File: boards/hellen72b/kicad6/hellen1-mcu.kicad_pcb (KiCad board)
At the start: 2 copper layers, 46.5 x 37.3 mm, 91 parts, among them J101 TC2030-IDC-NL, J102 Net Tie, M101 Module:mcu/0.1, U101 AMS1117-3.3, U102 LMV324IPWR, U103 AP2337SA-7, U104 LMV324IPWR, U105 STM32F427IGT6, U106 LMV324IPWR, U107 LMV324IPWR, U108 LMV324IPWR, U109 LMV324IPWR, U111 XC6206P332MR, Y101 32.768 kHz, Y102 8.0 MHz

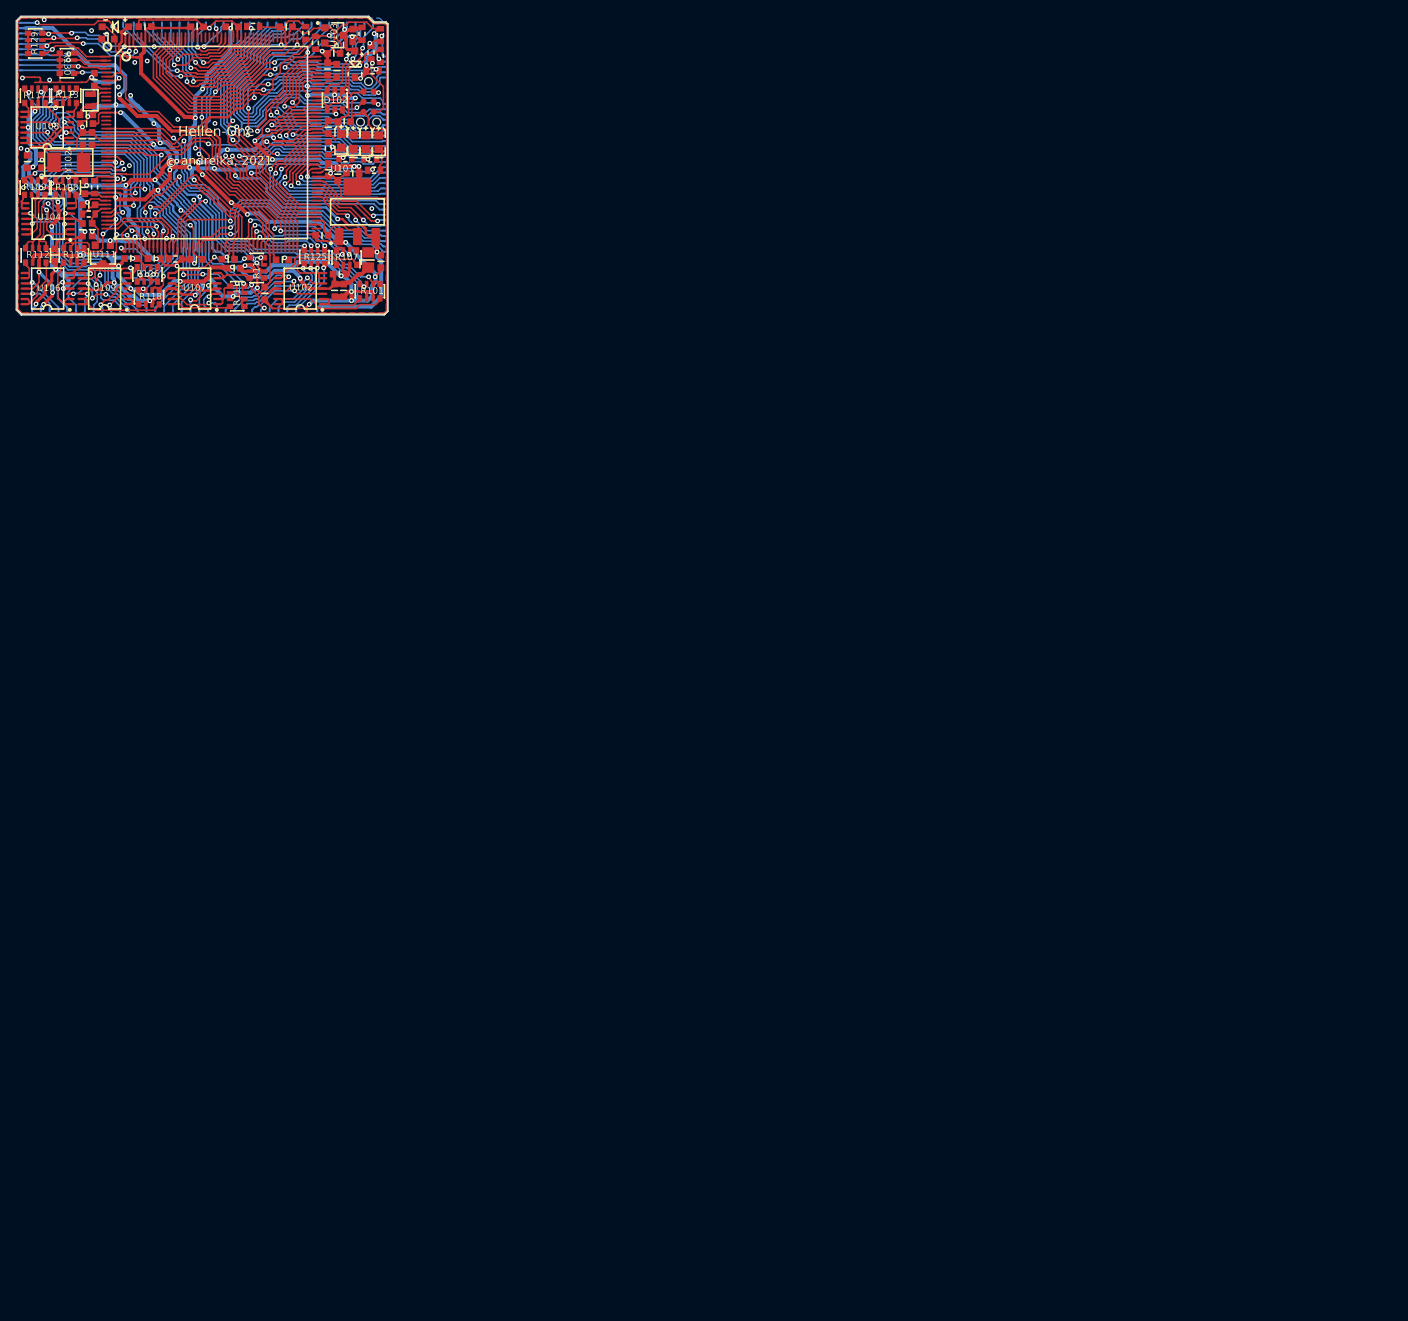
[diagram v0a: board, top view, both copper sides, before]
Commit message: update exported kicad files after refactoring
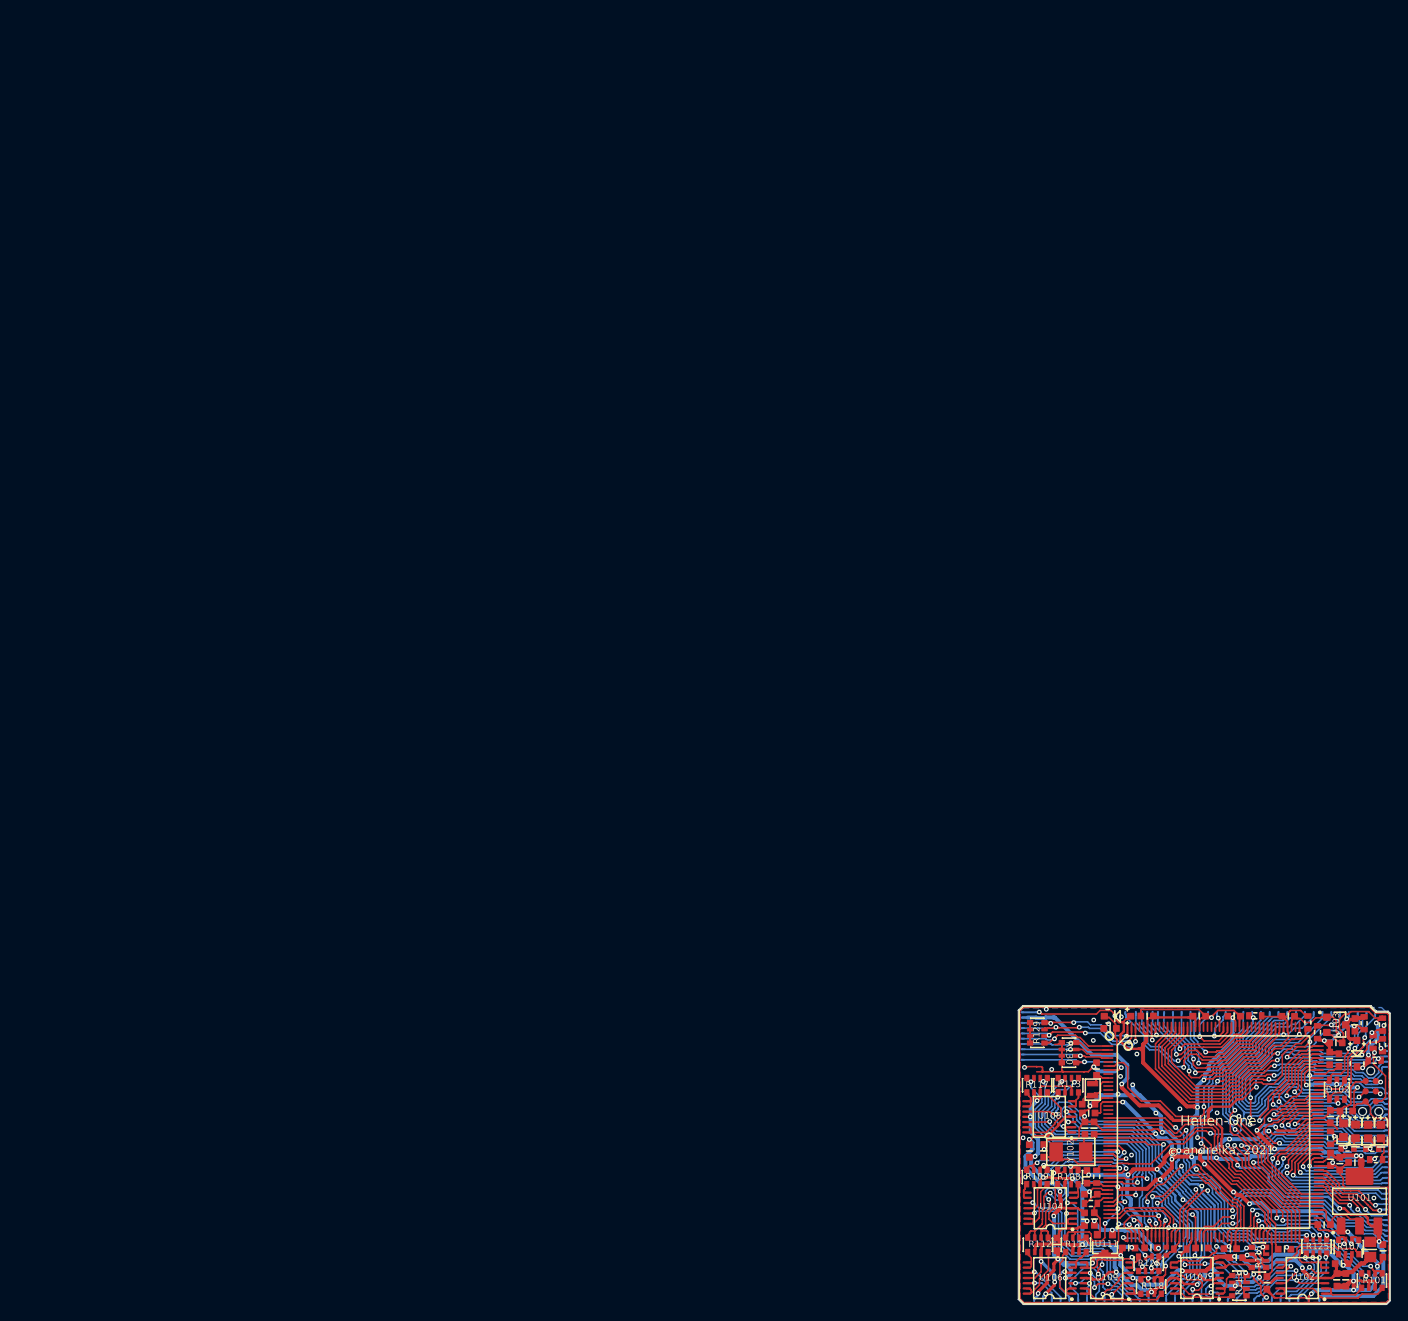
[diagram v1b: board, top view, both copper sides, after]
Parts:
- added R131: 0, General.pcblib:Res, F.Cu at (143.8, 117.0)
- moved R128 176.3 mm to (145.5, 116.8)
- moved C128 176.3 mm to (148.2, 116.6), turned to 180 degrees
- moved U107 176.1 mm to (147.6, 120.4)
- moved C121 176.0 mm to (164.3, 105.5)
- moved D105 176.0 mm to (165.9, 101.9)
- moved R105 176.0 mm to (170.8, 88.7)
- moved R129 176.0 mm to (127.6, 89.7)
- moved U103 176.0 mm to (165.0, 88.7)
- moved C101 176.0 mm to (166.3, 99.5)
- moved C104 176.0 mm to (165.4, 106.1)
- moved C107 176.0 mm to (165.7, 118.6)
- moved C116 176.0 mm to (134.0, 98.7)
- moved C117 176.0 mm to (134.1, 99.8)
- moved C120 176.0 mm to (130.1, 116.2)
- moved C132 176.0 mm to (133.6, 101.7)
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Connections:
- M101 pad N10: IO5 -> SPI3_MISO
- M101 pad N11: IO6 -> SPI3_MOSI
- M101 pad N12: IO7 -> IO5
- M101 pad N13: IO8 -> IO6
- M101 pad N14: V33 -> IO7
- M101 pad N15: VBAT -> IO8
- M101 pad N16: I2C_SDA -> V33
- M101 pad N17: I2C_SCL -> VBAT
- M101 pad N18: SPI_SD_SCK -> I2C_SDA
- M101 pad N19: SPI_SD_MISO -> I2C_SCL
- M101 pad N20: SPI_SD_MOSI -> SPI_SD_SCK
- M101 pad N21: SPI_SD_CS -> SPI_SD_MISO
- M101 pad N22: nReset -> SPI_SD_MOSI
- M101 pad N23: SWCLK -> SPI_SD_CS
- M101 pad N24: SWDIO -> nReset
- M101 pad N25: SWO -> SWCLK
- M101 pad N26: BOOT0 -> SWDIO
- M101 pad N27: VBUS -> SWO
- M101 pad N28: USBP -> BOOT0
- M101 pad N29: USBM -> VBUS
- M101 pad N30: USBID -> USBP
- M101 pad N4: UART_TX -> UART8_TX
- M101 pad N5: UART_RX -> UART8_RX
- M101 pad N6: IO1 -> UART2_TX
- M101 pad N7: IO2 -> UART2_RX
- M101 pad N8: IO3 -> SPI3_CS
- M101 pad N9: IO4 -> SPI3_SCK
- R128 pad 2: A22 -> BOOT1
- U105 pad 138: (no net) -> SPI3_CS
- U105 pad 139: (no net) -> SPI3_SCK
- U105 pad 140: IO1 -> SPI3_MISO
- U105 pad 141: IO2 -> SPI3_MOSI
- U105 pad 144: IO3 -> (no net)
- U105 pad 145: IO4 -> (no net)
- U105 pad 147: UART_TX -> UART2_TX
- U105 pad 150: UART_RX -> UART2_RX
- U105 pad 169: (no net) -> UART8_RX
- U105 pad 170: (no net) -> UART8_TX
- U105 pad 58: A22 -> BOOT1
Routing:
- net SPI3_CS: track 0.00 -> 23.6 mm, vias 0 -> 1
- net IO1: track 22.3 -> 0.00 mm, vias 1 -> 0
- net SPI3_SCK: track 0.00 -> 21.4 mm, vias 0 -> 1
- net IO2: track 20.3 -> 0.00 mm, vias 1 -> 0
- net SPI3_MISO: track 0.00 -> 19.6 mm, vias 0 -> 1
- net SPI3_MOSI: track 0.00 -> 17.5 mm, vias 0 -> 1
- net UART_TX: track 17.1 -> 0.00 mm, vias 1 -> 0
- net UART2_TX: track 0.00 -> 16.6 mm, vias 0 -> 1
- net IO3: track 16.5 -> 0.00 mm, vias 1 -> 0
- net IO4: track 14.2 -> 0.00 mm, vias 1 -> 0
- net UART_RX: track 13.8 -> 0.00 mm, vias 1 -> 0
- net UART2_RX: track 0.00 -> 13.7 mm, vias 0 -> 1
- net UART8_TX: track 0.00 -> 5.63 mm, vias 0 -> 1
- net UART8_RX: track 0.00 -> 4.33 mm, vias 0 -> 1
- net GND: track 293.3 -> 289.7 mm, vias 57 -> 56
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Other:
- board size 46.5 x 37.3 mm -> 46.5 x 37.4 mm
